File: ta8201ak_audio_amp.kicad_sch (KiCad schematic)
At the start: 16 parts, among them J1 INPUT, J2 OUTPUT, J3 POWER, U1 TA8201AK

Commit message: 抵抗560Ωを追加Cを3.3uF,33uFに変更
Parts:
- added R3: 560, Resistor_THT:R_Axial_DIN0516_L15.5mm_D5.0mm_P7.62mm_Vertical, symbol Device:R
- C1: value 4.7uF -> 3.3uF
- C2: value 47uF -> 33uF
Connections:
- net at U1.2 (NF): now also R3.1; no longer C2.1
- new net: C2.1, R3.2
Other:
- moved on the sheet: C2
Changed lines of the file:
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@@
+	(wire
+		(pts
+			(xy 135.89 119.38) (xy 135.89 121.92)
+		)
+		(stroke
+			(width 0)
+			(type default)
+		)
+	)
+	(wire
+		(pts
+			(xy 135.89 127) (xy 135.89 128.27)
+		)
+		(stroke
+			(width 0)
+			(type default)
+		)
+	)
 	(wire
 		(pts
@@
 	(wire
 		(pts
+			(xy 135.89 107.95) (xy 135.89 111.76)
+		)
+		(stroke
+			(width 0)
+			(type default)
+		)
+	)
+	(wire
+		(pts
 			(xy 198.12 106.68) (xy 198.12 107.95)
 		)
@@
 	(wire
 		(pts
-			(xy 134.62 107.95) (xy 140.97 107.95)
-		)
-		(stroke
-			(width 0)
-			(type default)
-		)
-	)
-	(wire
-		(pts
 			(xy 185.42 115.57) (xy 185.42 121.92)
 		)
@@
 		(pts
 			(xy 185.42 107.95) (xy 198.12 107.95)
+		)
+		(stroke
+			(width 0)
+			(type default)
+		)
+	)
+	(wire
+		(pts
+			(xy 135.89 107.95) (xy 140.97 107.95)
 		)
 		(stroke
@@
 				(path "/3e27d207-50b8-40b2-b752-3d08c7aa128e"
 					(reference "C3")
+					(unit 1)
+				)
+			)
+		)
+	)
+	(symbol
+		(lib_id "Device:R")
+		(at 135.89 115.57 0)
+		(unit 1)
+		(exclude_from_sim no)
+		(in_bom yes)
+		(on_board yes)
+		(dnp no)
+		(fields_autoplaced yes)
+		(property "Reference" "R3"
+			(at 138.43 114.2999 0)
+			(effects
+				(font
+					(size 1.27 1.27)
+				)
+				(justify left)
+			)
+		)
+		(property "Value" "560"
+			(at 138.43 116.8399 0)
+			(effects
+				(font
+					(size 1.27 1.27)
+				)
+				(justify left)
+			)
+		)
+		(property "Footprint" "Resistor_THT:R_Axial_DIN0516_L15.5mm_D5.0mm_P7.62mm_Vertical"
+			(at 134.112 115.57 90)
+			(effects
+				(font
+					(size 1.27 1.27)
+				)
+				(hide yes)
+			)
+		)
+		(property "Datasheet" "~"
+			(at 135.89 115.57 0)
+			(effects
+				(font
+					(size 1.27 1.27)
+				)
+				(hide yes)
+			)
+		)
+		(property "Description" "Resistor"
+			(at 135.89 115.57 0)
+			(effects
+				(font
+					(size 1.27 1.27)
+				)
+				(hide yes)
+			)
+		)
+		(pin "1"
+		)
+		(pin "2"
+		)
+		(instances
+			(project "ta8201ak_audio_amp"
+				(path "/3e27d207-50b8-40b2-b752-3d08c7aa128e"
+					(reference "R3")
 					(unit 1)
 				)
@@
 	(symbol
 		(lib_id "Device:C_Small_US")
-		(at 134.62 110.49 0)
+		(at 135.89 124.46 0)
 		(unit 1)
 		(exclude_from_sim no)
@@
 		(fields_autoplaced yes)
 		(property "Reference" "C2"
-			(at 137.16 109.3469 0)
-			(effects
-				(font
-					(size 1.27 1.27)
-				)
-				(justify left)
-			)
-		)
-		(property "Value" "47uF"
-			(at 137.16 111.8869 0)
+			(at 138.43 123.3169 0)
+			(effects
+				(font
+					(size 1.27 1.27)
+				)
+				(justify left)
+			)
+		)
+		(property "Value" "33uF"
+			(at 138.43 125.8569 0)
 			(effects
 				(font
@@
 		)
 		(property "Footprint" "Capacitor_THT:CP_Radial_D5.0mm_P2.50mm"
-			(at 134.62 110.49 0)
+			(at 135.89 124.46 0)
 			(effects
 				(font
@@
 		)
 		(property "Datasheet" ""
-			(at 134.62 110.49 0)
+			(at 135.89 124.46 0)
 			(effects
 				(font
@@
 		)
 		(property "Description" "capacitor, small US symbol"
-			(at 134.62 110.49 0)
+			(at 135.89 124.46 0)
 			(effects
 				(font
@@
 			)
 		)
-		(property "Value" "4.7uF"
+		(property "Value" "3.3uF"
 			(at 137.414 103.378 90)
 			(effects
@@
 	(symbol
 		(lib_id "power:GND")
-		(at 134.62 113.03 0)
+		(at 135.89 128.27 0)
 		(unit 1)
 		(exclude_from_sim no)
@@
 		(fields_autoplaced yes)
 		(property "Reference" "#PWR01"
-			(at 134.62 119.38 0)
+			(at 135.89 134.62 0)
 			(effects
 				(font
@@
 		)
 		(property "Value" "GND"
-			(at 134.62 118.11 0)
+			(at 135.89 133.35 0)
 			(effects
 				(font
@@
 		)
 		(property "Footprint" ""
-			(at 134.62 113.03 0)
+			(at 135.89 128.27 0)
 			(effects
 				(font
@@
 		)
 		(property "Datasheet" ""
-			(at 134.62 113.03 0)
+			(at 135.89 128.27 0)
 			(effects
 				(font
@@
 		)
 		(property "Description" "Power symbol creates a global label with name \"GND\" , ground"
-			(at 134.62 113.03 0)
-			(effects
-				(font
+			(at 135.89 128.27 0)
+			(effects
+				(font

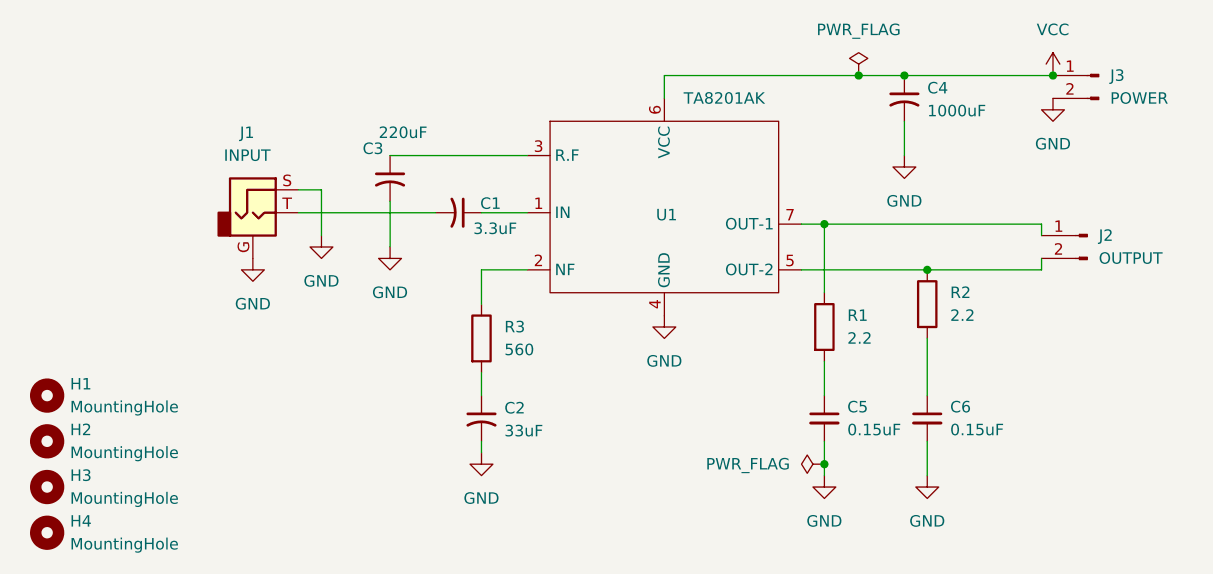
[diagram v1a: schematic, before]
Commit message: 配置変更、アッテネーター追加、ベタ追加。
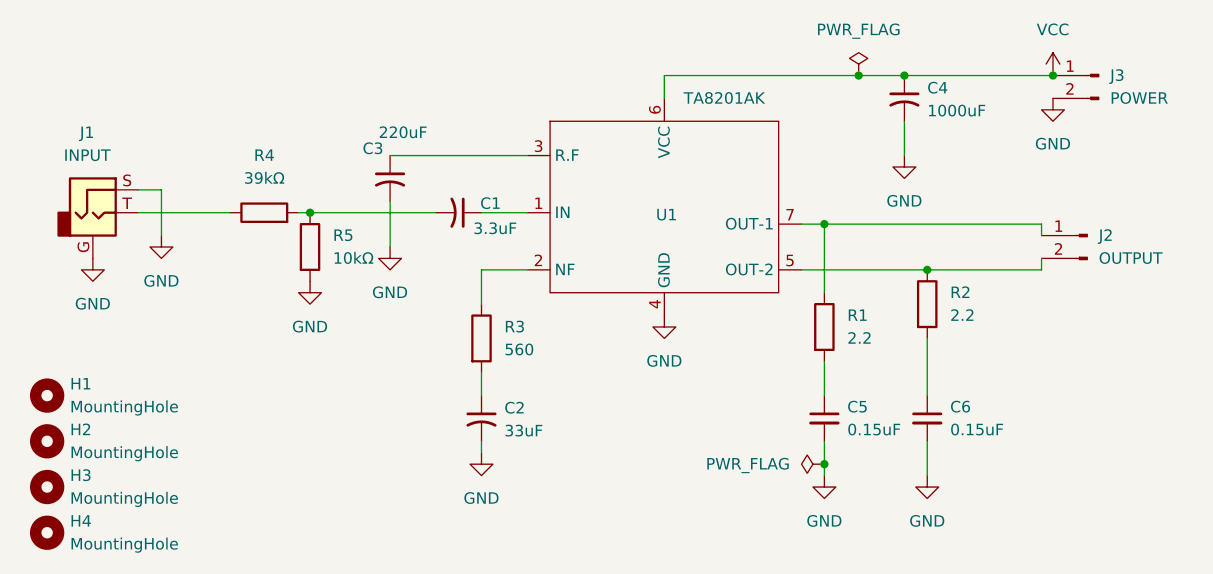
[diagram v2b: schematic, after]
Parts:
- added R4: 39kΩ, Resistor_THT:R_Axial_DIN0516_L15.5mm_D5.0mm_P7.62mm_Vertical, symbol Device:R
- added R5: 10kΩ, Resistor_THT:R_Axial_DIN0516_L15.5mm_D5.0mm_P7.62mm_Vertical, symbol Device:R
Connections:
- net GND: now also R5.2
- net at J1.T: now also R4.1; no longer C1.2
- new net: C1.2, R4.2, R5.1
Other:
- moved on the sheet: J1

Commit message: 電解コンデンサの足幅修正
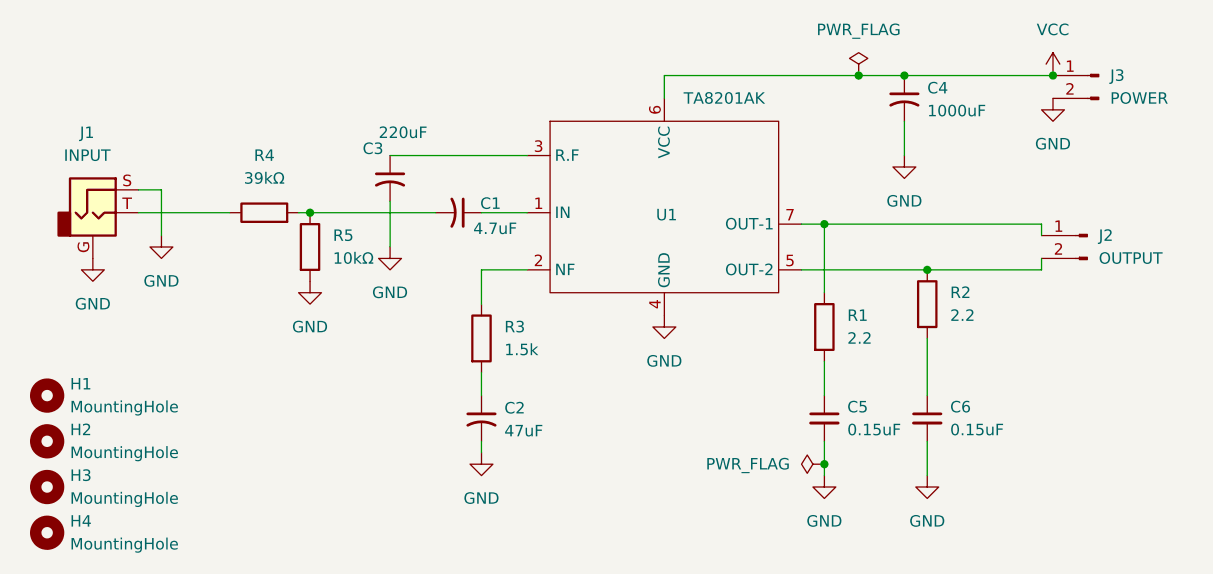
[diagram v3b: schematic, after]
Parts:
- C1: value 3.3uF -> 4.7uF
- C2: value 33uF -> 47uF
- C3: footprint Capacitor_THT:CP_Radial_D8.0mm_P2.50mm -> Capacitor_THT:CP_Radial_D8.0mm_P5.00mm
- R3: value 560 -> 1.5k
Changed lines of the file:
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@@
 			)
 		)
-		(property "Footprint" "Capacitor_THT:CP_Radial_D8.0mm_P2.50mm"
+		(property "Footprint" "Capacitor_THT:CP_Radial_D8.0mm_P5.00mm"
 			(at 125.73 97.79 0)
 			(effects
@@
 			)
 		)
-		(property "Value" "560"
+		(property "Value" "1.5k"
 			(at 138.43 116.8399 0)
 			(effects
@@
 			)
 		)
-		(property "Value" "33uF"
+		(property "Value" "47uF"
 			(at 138.43 125.8569 0)
 			(effects
@@
 			)
 		)
-		(property "Value" "3.3uF"
+		(property "Value" "4.7uF"
 			(at 137.414 103.378 90)
 			(effects

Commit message: 発振が酷いので部品配置を変更して解決できた 2.2Ω以外の抵抗は無くても利得が大きすぎるといったことは無いとおもう。
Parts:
- R1, R2: footprint Resistor_THT:R_Axial_DIN0516_L15.5mm_D5.0mm_P7.62mm_Vertical -> Resistor_THT:R_Axial_DIN0414_L11.9mm_D4.5mm_P5.08mm_Vertical
- R3, R4, R5: footprint Resistor_THT:R_Axial_DIN0516_L15.5mm_D5.0mm_P7.62mm_Vertical -> Resistor_THT:R_Axial_DIN0411_L9.9mm_D3.6mm_P7.62mm_Vertical
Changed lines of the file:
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@@
 			)
 		)
-		(property "Footprint" "Resistor_THT:R_Axial_DIN0516_L15.5mm_D5.0mm_P7.62mm_Vertical"
+		(property "Footprint" "Resistor_THT:R_Axial_DIN0414_L11.9mm_D4.5mm_P5.08mm_Vertical"
 			(at 183.642 111.76 90)
 			(effects
@@
 			)
 		)
-		(property "Footprint" "Resistor_THT:R_Axial_DIN0516_L15.5mm_D5.0mm_P7.62mm_Vertical"
+		(property "Footprint" "Resistor_THT:R_Axial_DIN0411_L9.9mm_D3.6mm_P7.62mm_Vertical"
 			(at 134.112 115.57 90)
 			(effects
@@
 			)
 		)
-		(property "Footprint" "Resistor_THT:R_Axial_DIN0516_L15.5mm_D5.0mm_P7.62mm_Vertical"
+		(property "Footprint" "Resistor_THT:R_Axial_DIN0411_L9.9mm_D3.6mm_P7.62mm_Vertical"
 			(at 111.76 103.378 90)
 			(effects
@@
 			)
 		)
-		(property "Footprint" "Resistor_THT:R_Axial_DIN0516_L15.5mm_D5.0mm_P7.62mm_Vertical"
+		(property "Footprint" "Resistor_THT:R_Axial_DIN0414_L11.9mm_D4.5mm_P5.08mm_Vertical"
 			(at 172.212 114.3 90)
 			(effects
@@
 			)
 		)
-		(property "Footprint" "Resistor_THT:R_Axial_DIN0516_L15.5mm_D5.0mm_P7.62mm_Vertical"
+		(property "Footprint" "Resistor_THT:R_Axial_DIN0411_L9.9mm_D3.6mm_P7.62mm_Vertical"
 			(at 115.062 105.41 90)
 			(effects

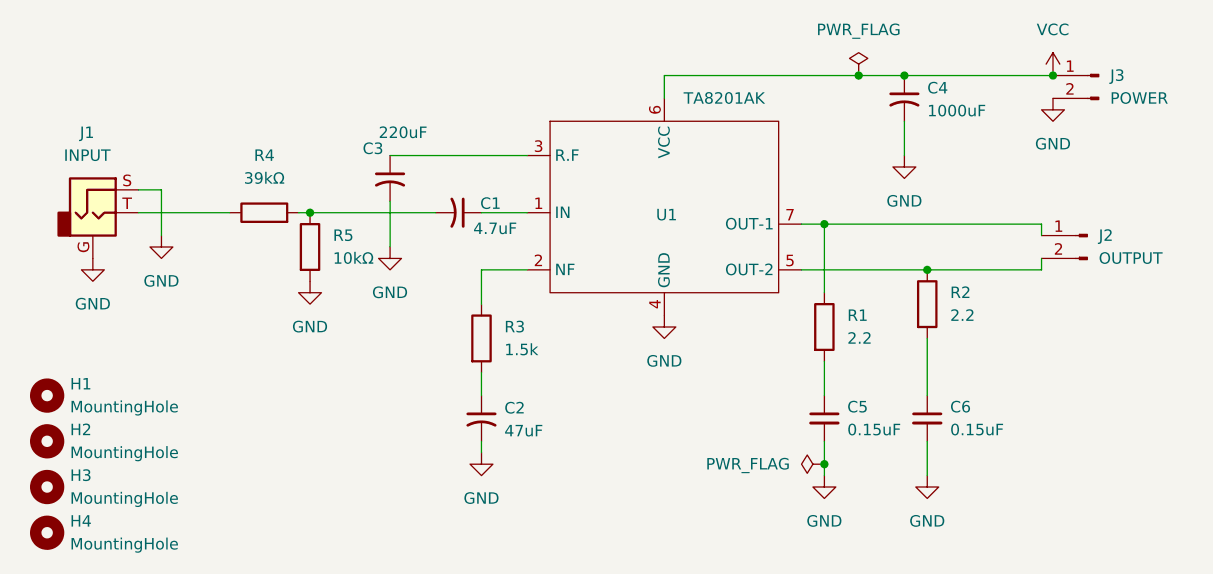
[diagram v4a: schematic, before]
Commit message: 発振が酷いので配置の見直しと配線を太くした
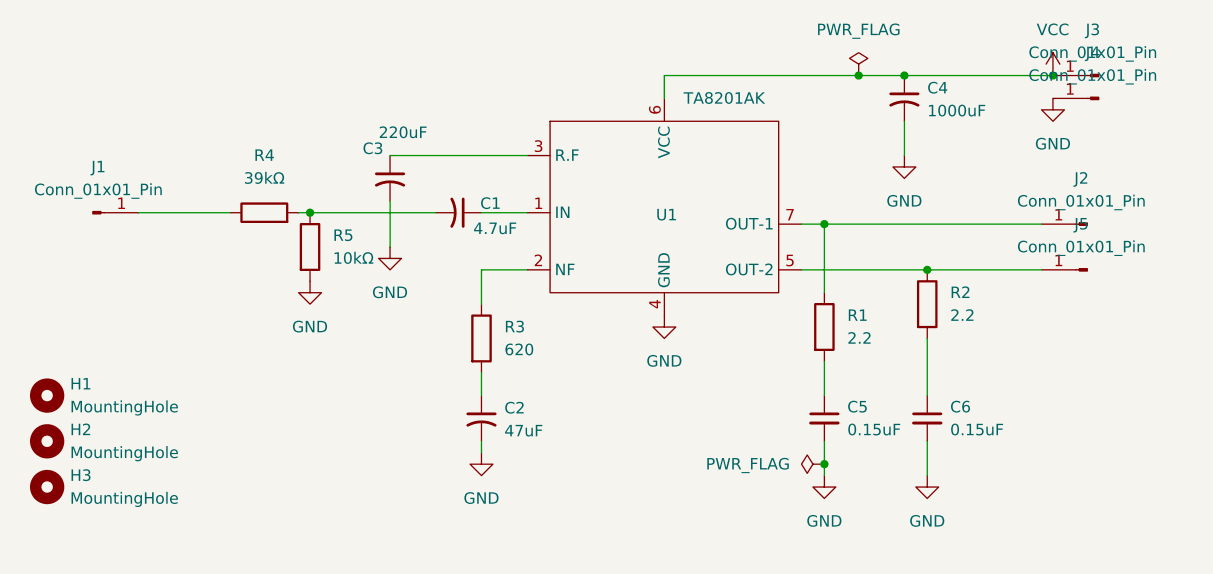
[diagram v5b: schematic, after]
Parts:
- removed H4: MountingHole, MountingHole:MountingHole_3.2mm_M3, symbol Mechanical:MountingHole
- removed J1: INPUT, Connector_JST:JST_XH_B2B-XH-A_1x02_P2.50mm_Vertical, symbol Connector_Audio:AudioJack2_Ground
- removed J2: OUTPUT, Connector_JST:JST_XH_B2B-XH-A_1x02_P2.50mm_Vertical, symbol Connector:Conn_01x02_Pin
- removed J3: POWER, Connector_JST:JST_XH_B2B-XH-A_1x02_P2.50mm_Vertical, symbol Connector:Conn_01x02_Pin
- added J1, J2, J3, J4, J5: Conn_01x01_Pin, Connector_PinHeader_2.54mm:PinHeader_1x01_P2.54mm_Vertical, symbol Connector:Conn_01x01_Pin
- R3: value 1.5k -> 620
- U1: footprint @MyLibrary:TA8201AK -> MyLibrary:TA8201AK
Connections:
- net GND: now also J4.1 (Pin_1)
- net VCC: now also J3.1 (Pin_1)
- net at R4.1: now also J1.1 (Pin_1)
- net at R2.1, U1.5 (OUT-2): now also J5.1 (Pin_1)
- net at R1.1, U1.7 (OUT-1): now also J2.1 (Pin_1)

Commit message: 修正
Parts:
- R3, R4, R5: footprint Resistor_THT:R_Axial_DIN0411_L9.9mm_D3.6mm_P7.62mm_Vertical -> Resistor_THT:R_Axial_DIN0411_L9.9mm_D3.6mm_P5.08mm_Vertical
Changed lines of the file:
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@@
 			)
 		)
-		(property "Footprint" "Resistor_THT:R_Axial_DIN0411_L9.9mm_D3.6mm_P7.62mm_Vertical"
+		(property "Footprint" "Resistor_THT:R_Axial_DIN0411_L9.9mm_D3.6mm_P5.08mm_Vertical"
 			(at 134.112 115.57 90)
 			(effects
@@
 			)
 		)
-		(property "Footprint" "Resistor_THT:R_Axial_DIN0411_L9.9mm_D3.6mm_P7.62mm_Vertical"
+		(property "Footprint" "Resistor_THT:R_Axial_DIN0411_L9.9mm_D3.6mm_P5.08mm_Vertical"
 			(at 111.76 103.378 90)
 			(effects
@@
 			)
 		)
-		(property "Footprint" "Resistor_THT:R_Axial_DIN0411_L9.9mm_D3.6mm_P7.62mm_Vertical"
+		(property "Footprint" "Resistor_THT:R_Axial_DIN0411_L9.9mm_D3.6mm_P5.08mm_Vertical"
 			(at 115.062 105.41 90)
 			(effects

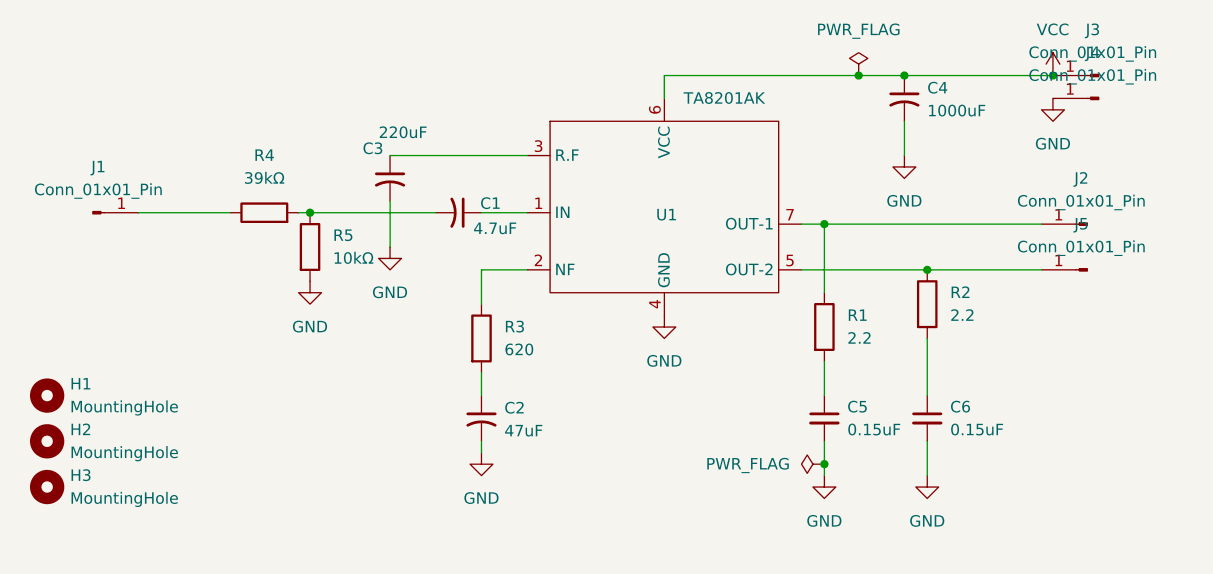
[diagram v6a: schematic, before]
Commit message: 配置と配線を修正
配線の修正
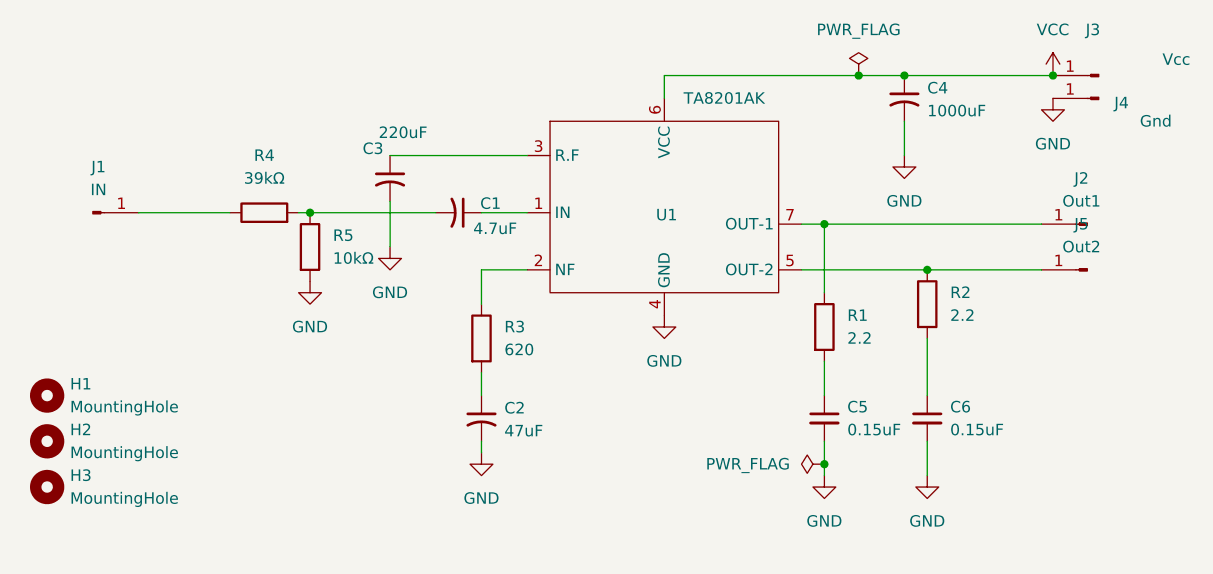
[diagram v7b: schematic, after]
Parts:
- J1: value Conn_01x01_Pin -> IN
- J2: value Conn_01x01_Pin -> Out1
- J3: value Conn_01x01_Pin -> Vcc
- J4: value Conn_01x01_Pin -> Gnd
- J5: value Conn_01x01_Pin -> Out2
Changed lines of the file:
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@@
 			)
 		)
-		(property "Value" "Conn_01x01_Pin"
+		(property "Value" "IN"
 			(at 93.345 99.06 0)
 			(effects
@@
 		(on_board yes)
 		(dnp no)
-		(fields_autoplaced yes)
 		(property "Reference" "J3"
 			(at 203.835 81.28 0)
@@
 			)
 		)
-		(property "Value" "Conn_01x01_Pin"
-			(at 203.835 83.82 0)
+		(property "Value" "Vcc"
+			(at 213.106 84.582 0)
 			(effects
 				(font
@@
 			)
 		)
-		(property "Value" "Conn_01x01_Pin"
+		(property "Value" "Out1"
 			(at 202.565 100.33 0)
 			(effects
@@
 			)
 		)
-		(property "Value" "Conn_01x01_Pin"
+		(property "Value" "Out2"
 			(at 202.565 105.41 0)
 			(effects
@@
 		(on_board yes)
 		(dnp no)
-		(fields_autoplaced yes)
 		(property "Reference" "J4"
-			(at 203.835 83.82 0)
-			(effects
-				(font
-					(size 1.27 1.27)
-				)
-			)
-		)
-		(property "Value" "Conn_01x01_Pin"
-			(at 203.835 86.36 0)
-			(effects
-				(font
+			(at 207.01 89.408 0)
+			(effects
+				(font
+					(size 1.27 1.27)
+				)
+			)
+		)
+		(property "Value" "Gnd"
+			(at 210.82 91.44 0)
+			(effects
+				(font

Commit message: 仕切り直す
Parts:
- removed U1: TA8201AK, MyLibrary:TA8201AK, symbol @MyLibrary:TA8201AK
- added U1: ~, MyLibrary:TA8201AK, symbol MyLibrary:TA8201AK
- C1: value 4.7uF -> 4.7u
- C2: value 47uF -> 47u
- C3: value 220uF -> 220u
- C4: value 1000uF -> 1000u
- C5, C6: value 0.15uF -> 0.15u
- R4: value 39kΩ -> 39k
- R5: value 10kΩ -> 1M
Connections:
- net GND: now also U1.4 (GND)
- net VCC: now also U1.6 (VCC)
- net at J5.1 (Pin_1), R2.1: now also U1.5 (OUT-2)
- net at C3.1: now also U1.3 (R.F)
- net at J2.1 (Pin_1), R1.1: now also U1.7 (OUT-1)
- net at R3.1: now also U1.2 (NF)
- net at C1.1: now also U1.1 (IN)
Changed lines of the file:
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@@
 			)
 		)
-		(property "Value" "0.15uF"
+		(property "Value" "0.15u"
 			(at 187.96 125.7362 0)
 			(effects
@@
 			)
 		)
-		(property "Value" "1000uF"
+		(property "Value" "1000u"
 			(at 185.42 90.2969 0)
 			(effects
@@
 			)
 		)
-		(property "Value" "220uF"
+		(property "Value" "220u"
 			(at 124.46 92.71 0)
 			(effects
@@
 			)
 		)
-		(property "Value" "39kΩ"
+		(property "Value" "39k"
 			(at 111.76 97.79 90)
 			(effects
@@
 			)
 		)
-		(property "Value" "47uF"
+		(property "Value" "47u"
 			(at 138.43 125.8569 0)
 			(effects
@@
 			)
 		)
-		(property "Value" "4.7uF"
+		(property "Value" "4.7u"
 			(at 137.414 103.378 90)
 			(effects
@@
 			)
 		)
-		(property "Value" "10kΩ"
+		(property "Value" "1M"
 			(at 119.38 106.6799 0)
 			(effects
@@
 			)
 		)
-		(property "Value" "0.15uF"
+		(property "Value" "0.15u"
 			(at 176.53 125.7362 0)
 			(effects
@@
 	)
 	(symbol
-		(lib_id "@MyLibrary:TA8201AK")
+		(lib_id "MyLibrary:TA8201AK")
 		(at 156.21 101.6 0)
 		(unit 1)
@@
 					(size 1.27 1.27)
 				)
-			)
-		)
-		(property "Value" "TA8201AK"
+				(hide yes)
+			)
+		)
+		(property "Value" "~"
 			(at 158.3533 88.9 0)
 			(effects
@@
 			)
 		)
+		(pin "2"
+		)
+		(pin "4"
+		)
+		(pin "3"
+		)
+		(pin "7"
+		)
+		(pin "5"
+		)
 		(pin "6"
 		)
-		(pin "4"
-		)
-		(pin "5"
-		)
-		(pin "7"
-		)
-		(pin "2"
-		)
-		(pin "1"
-		)
-		(pin "3"
-		)
-		(instances
+		(pin "1"
+		)
+		(instances
